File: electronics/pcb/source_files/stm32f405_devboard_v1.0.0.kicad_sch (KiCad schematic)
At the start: 46 parts, among them J1 Screw_Terminal_01x02, J2 SWD, J3 USB_B_Micro, J4 Conn_01x04, J5 Conn_01x04, Q1 AO3401A, SW1 SW_SPDT, U1 STM32F405RGT6, U2 MP2359DJ-LF-Z-MS, U3 USBLC6-2SC6, Y1 16MHz

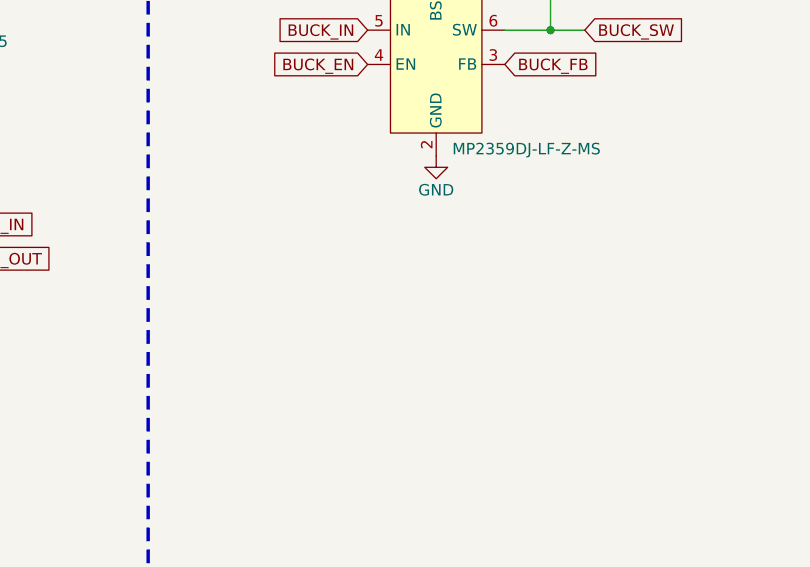
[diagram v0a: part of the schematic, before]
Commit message: Add regulator documentation and diagrams; remove obsolete images
- Created a new markdown file for regulator details including selection, features, applications, and specifications.
- Added diagrams for power delivery network and system architecture.
- Removed outdated image files that are no longer needed.
- Introduced a new markdown file for system specifications.
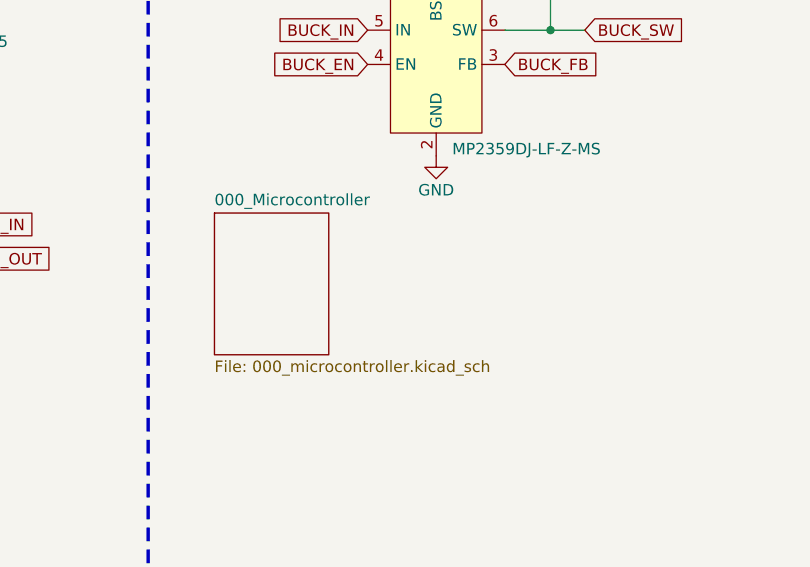
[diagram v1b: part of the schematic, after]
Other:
- added sheet 000_Microcontroller (000_microcontroller.kicad_sch)
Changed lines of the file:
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@@
+		)
+	)
+	(sheet
+		(at 156.972 151.13)
+		(size 12.7 15.748)
+		(exclude_from_sim no)
+		(in_bom yes)
+		(on_board yes)
+		(dnp no)
+		(fields_autoplaced yes)
+		(stroke
+			(width 0.1524)
+			(type solid)
+		)
+		(fill
+			(color 0 0 0 0.0000)
+		)
+		(property "Sheetname" "000_Microcontroller"
+			(at 156.972 150.4184 0)
+			(effects
+				(font
+					(size 1.27 1.27)
+				)
+				(justify left bottom)
+			)
+		)
+		(property "Sheetfile" "000_microcontroller.kicad_sch"
+			(at 156.972 167.4626 0)
+			(effects
+				(font
+					(size 1.27 1.27)
+				)
+				(justify left top)
+			)
+		)
+		(instances
+			(project "stm32f405_devboard_v1.0.0"
+				(path "/6b16d7e3-405f-4c62-a806-758d517aa001"
+					(page "2")
+				)
+			)
 		)
 	)

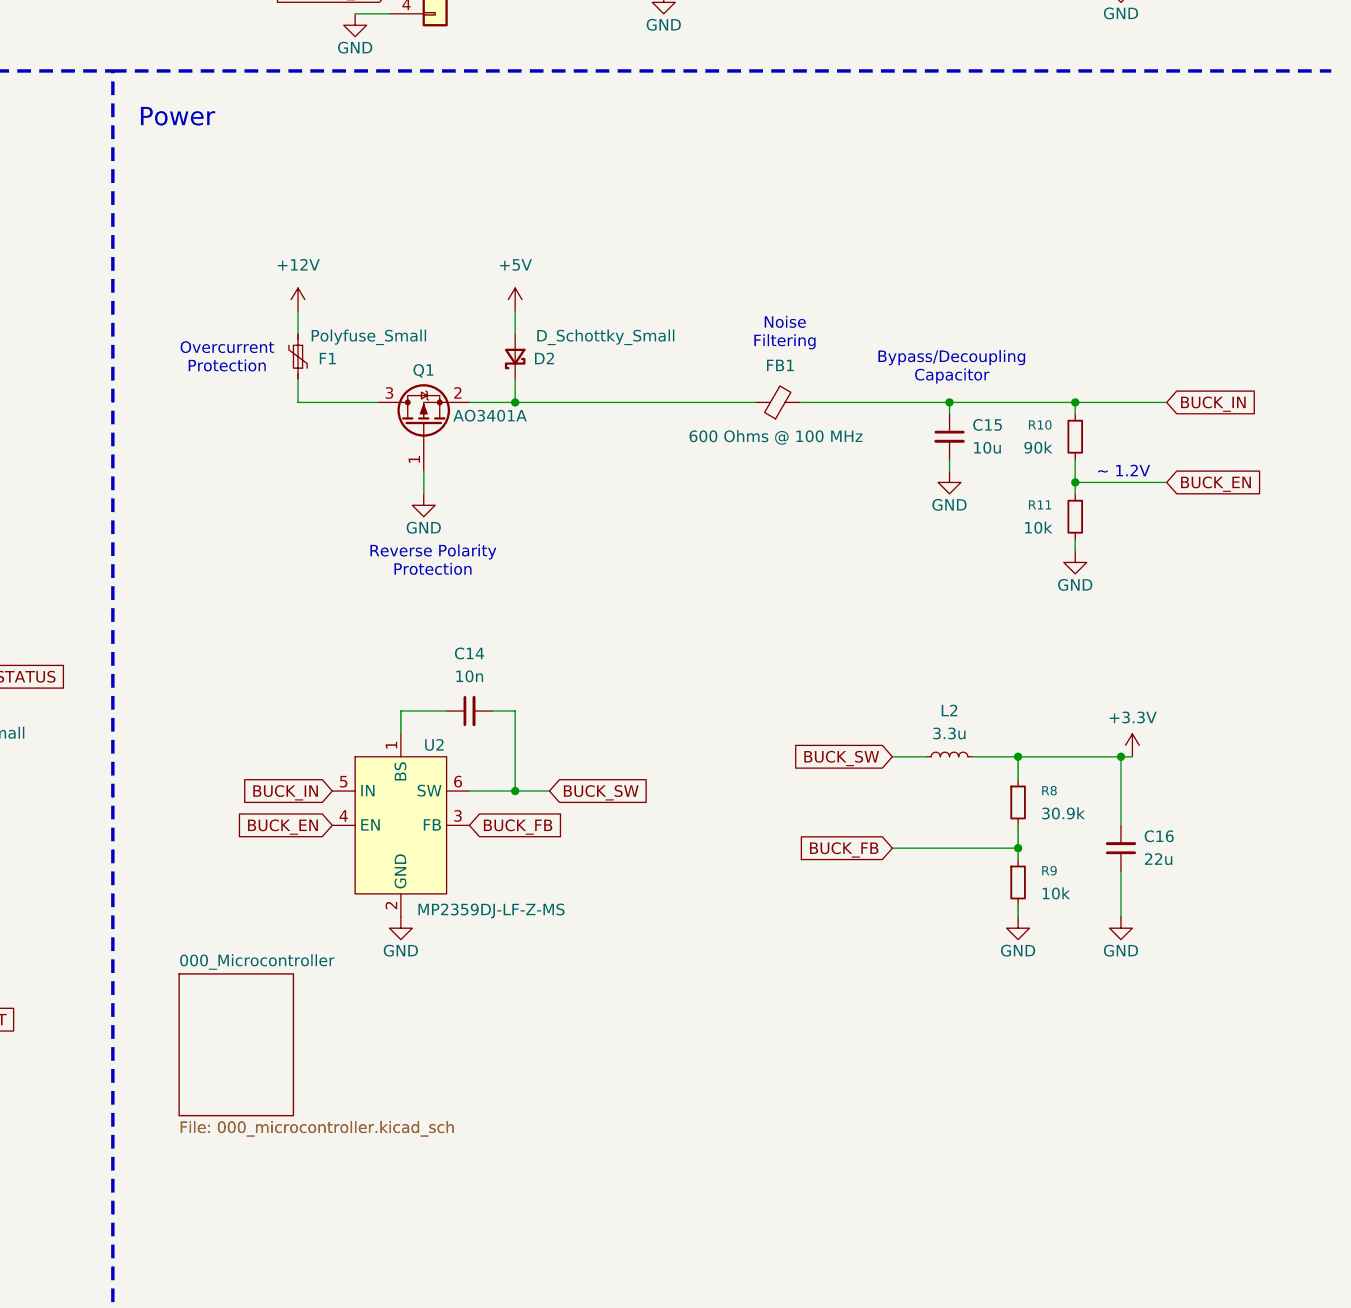
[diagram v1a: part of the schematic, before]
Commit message: Add mounting holes in schematic
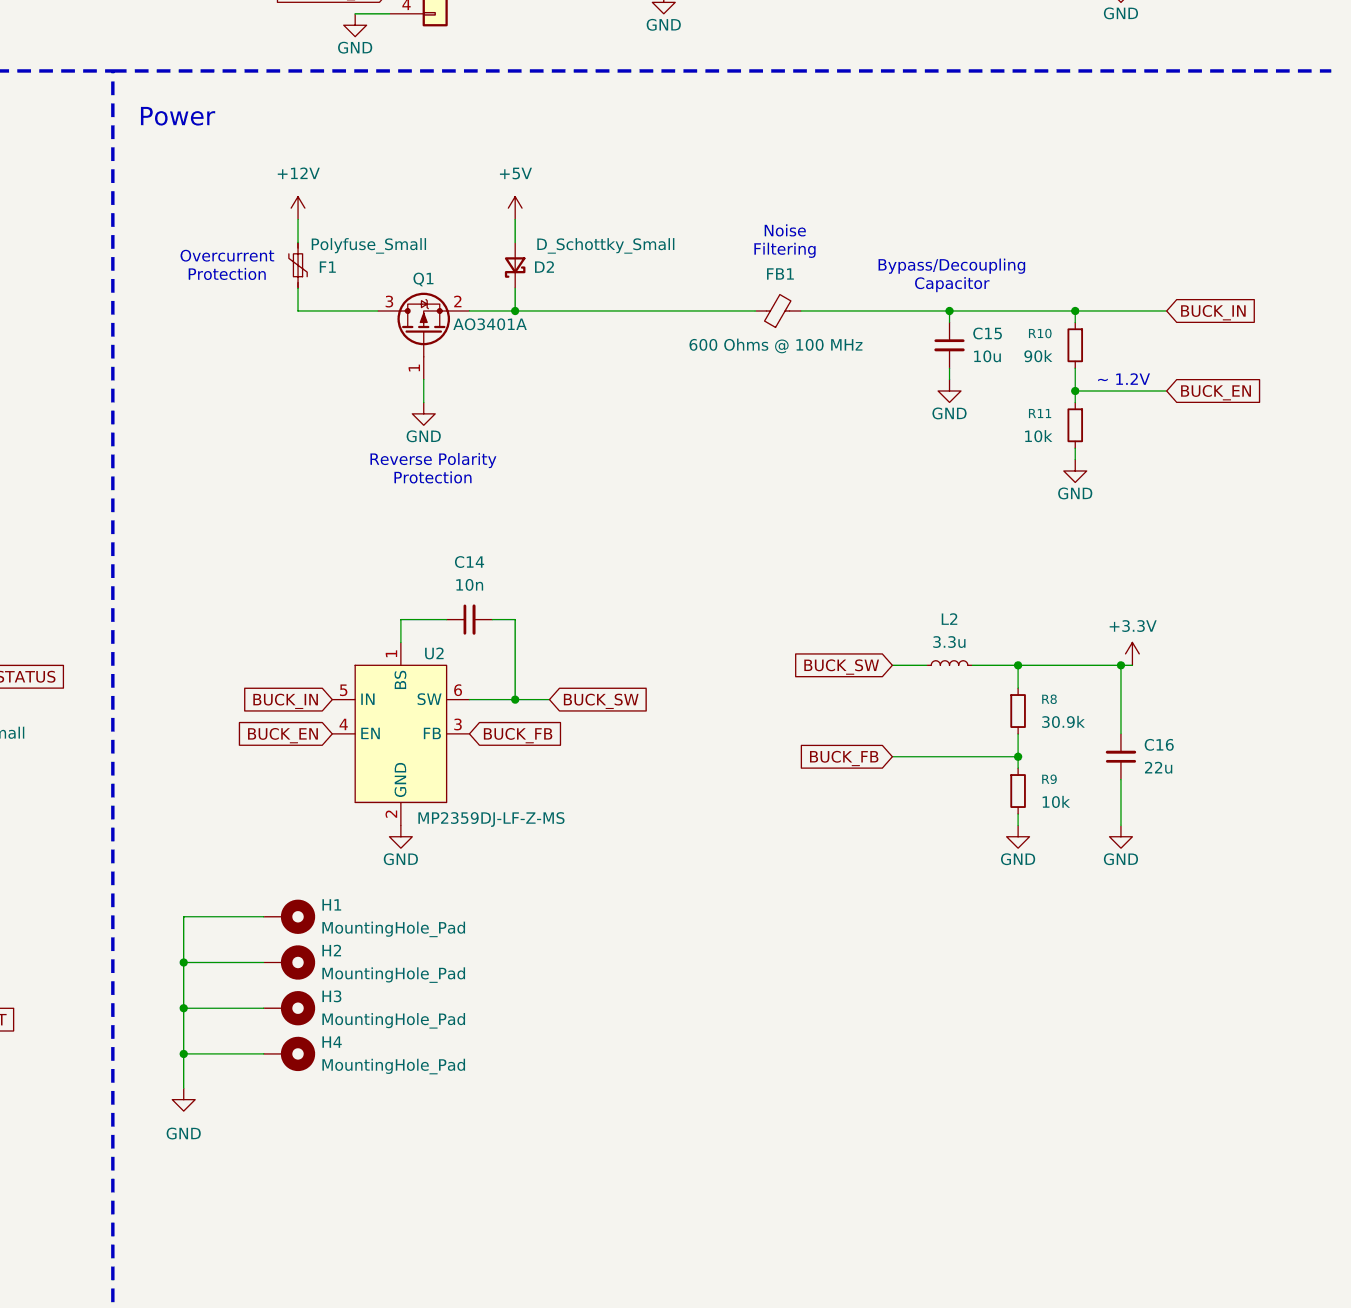
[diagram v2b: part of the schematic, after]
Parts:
- added H1, H2, H3, H4: MountingHole_Pad, symbol Mechanical:MountingHole_Pad
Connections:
- net GND: now also H1.1, H2.1, H3.1, H4.1
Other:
- removed sheet 000_Microcontroller
- moved on the sheet: C14, C15, C16, D2, F1, FB1, L2, Q1, R10, R11, R8, R9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

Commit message: MCU schematic section reorganized
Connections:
- net VCAP1: now reaches C1.1, U1.31 (VCAP_1)
- net VCAP2: now reaches C3.1, U1.47 (VCAP_2)
- net CONN_USB_D+: no longer names the net of J3.3 (D+), U3.1 (I/O1)
- net CONN_USB_D-: no longer names the net of J3.2 (D-), U3.3 (I/O2)
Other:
- note added: "Boot"
- note added: "Can I use other connector pins for the protocol?"
- note added: "External Clock"
- note added: "I2C Protocol"
- note added: "Internal LDO Regulator"
- note added: "MCU"
- note added: "Power Entry & Reverse Polarity"
- note added: "Power Led Indication"
- note added: "Serial Wire Debug (SWD)"
- note added: "USART Protocol"
- note added: "USB Interface"
- note removed: "Decoupling Caps"
- note removed: "Filtering"
- moved on the sheet: C1, C10, C11, C12, C13, C14, C15, C16, C2, C3, C4, C5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
